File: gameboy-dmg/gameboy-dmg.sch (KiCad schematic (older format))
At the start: 32 parts, among them J1 Conn_01x02, J2 Conn_01x02, J3 Conn_01x08, J4 Conn_01x02, J5 Raspberry_Pi_2_3, J6 Conn_01x09, J8 Conn_01x02, SW1 SW_DIP_x01, U1 MCP23017_SO

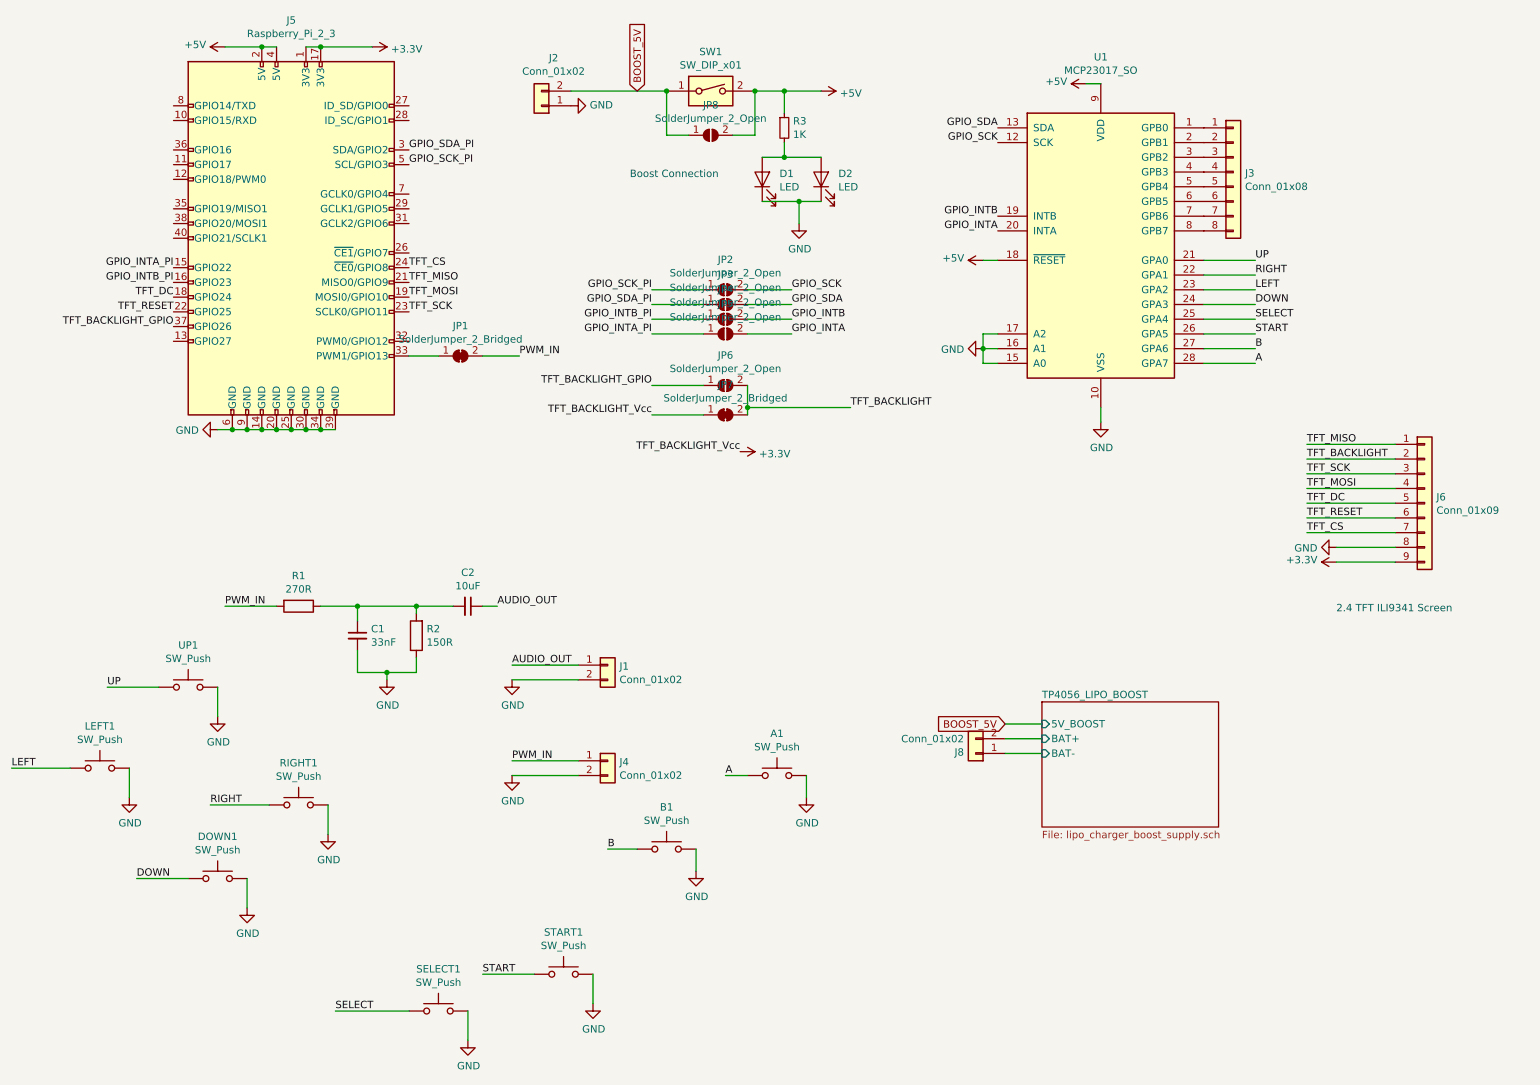
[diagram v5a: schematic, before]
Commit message: Moved buttons and audio to individual sheets and added audio amp
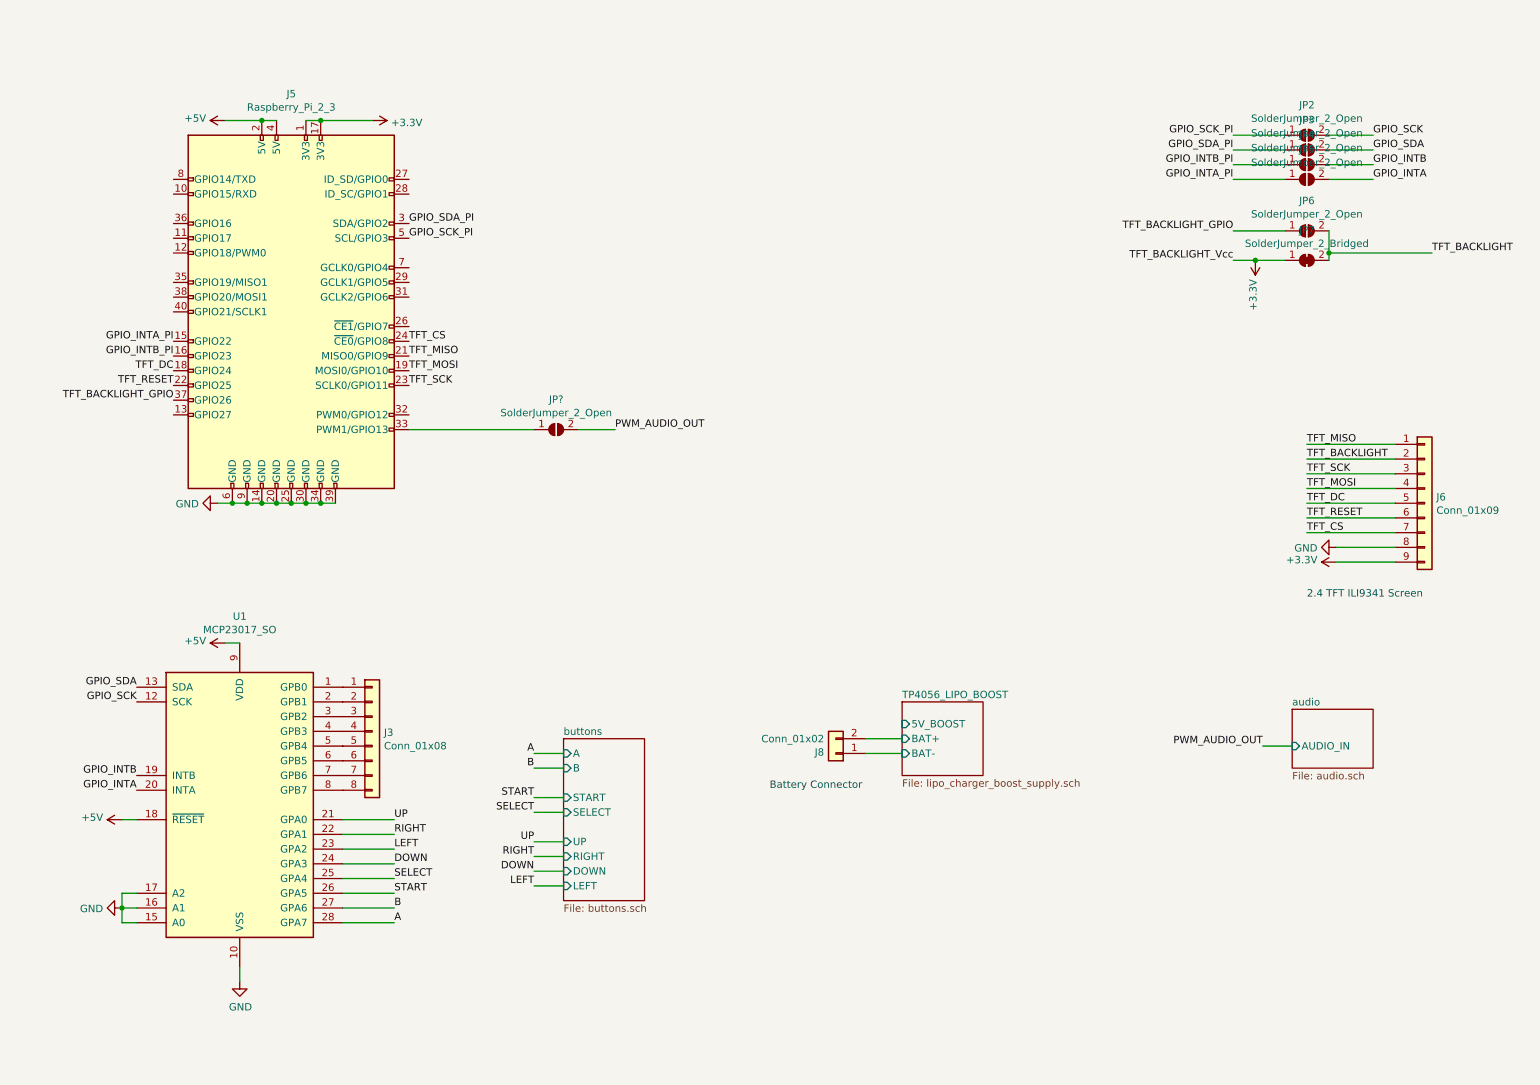
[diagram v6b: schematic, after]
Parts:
- removed A1, B1, DOWN1, LEFT1, RIGHT1, UP1: SW_Push, pad:GAMEBOY_BUTTON_PAD-D6MM, symbol Switch:SW_Push
- removed C1: 33nF, Capacitor_SMD:C_0603_1608Metric, symbol Device:C_Small
- removed C2: 10uF, Capacitor_THT:CP_Radial_D5.0mm_P2.00mm, symbol Device:C_Small
- removed D1: LED, LED_SMD:LED_0603_1608Metric, symbol Device:LED
- removed D2: LED, LED_THT:LED_D3.0mm, symbol Device:LED
- removed J1, J2, J4: Conn_01x02, Connector_PinHeader_2.54mm:PinHeader_1x02_P2.54mm_Vertical, symbol Connector_Generic:Conn_01x02
- removed JP1: SolderJumper_2_Bridged, Jumper:SolderJumper-2_P1.3mm_Bridged_RoundedPad1.0x1.5mm, symbol Jumper:SolderJumper_2_Bridged
- removed JP8: SolderJumper_2_Open, Jumper:SolderJumper-2_P1.3mm_Open_RoundedPad1.0x1.5mm, symbol Jumper:SolderJumper_2_Open
- removed R1: 270R, Resistor_SMD:R_0603_1608Metric, symbol Device:R
- removed R2: 150R, Resistor_SMD:R_0603_1608Metric, symbol Device:R
- removed R3: 1K, Resistor_SMD:R_0603_1608Metric, symbol Device:R_Small
- removed SELECT1, START1: SW_Push, pad:GAMEBOY_BUTTON_PAD-DUAL_D4MM, symbol Switch:SW_Push
- removed SW1: SW_DIP_x01, Connector_PinHeader_2.54mm:PinHeader_1x02_P2.54mm_Vertical, symbol Switch:SW_DIP_x01
- added JP?: SolderJumper_2_Open, Jumper:SolderJumper-2_P1.3mm_Open_RoundedPad1.0x1.5mm, symbol Jumper:SolderJumper_2_Open
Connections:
- net at J5.33 (PWM1/GPIO13): now also JP?.1 (A)
- new net PWM_AUDIO_OUT: JP?.2 (B)
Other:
- note added: "Battery Connector"
- note removed: "Boost Connection"
- moved on the sheet: J3, J5, J8, JP2, JP3, JP4, JP5, JP6, JP7, U1

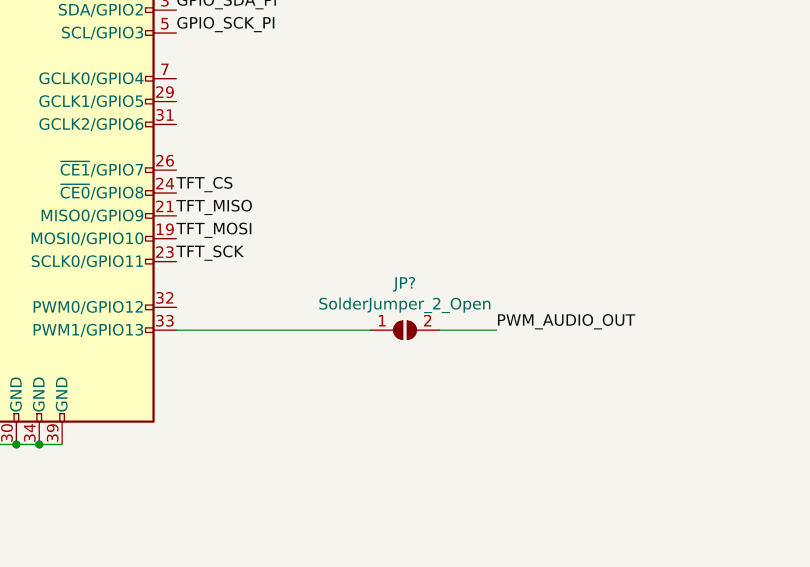
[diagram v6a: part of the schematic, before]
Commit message: Added unroputed and unchecked horizontal vol pot
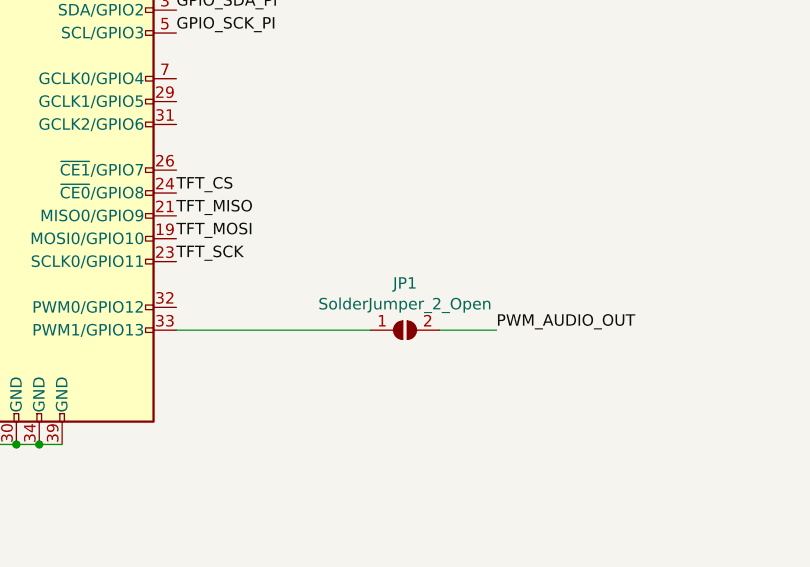
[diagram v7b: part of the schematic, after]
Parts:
- gave numbers to parts that had none: 1
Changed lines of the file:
@@
 	9050 2150 9250 2150
 $Comp
-L Jumper:SolderJumper_2_Open JP?
+L Jumper:SolderJumper_2_Open JP1
 U 1 1 5E850359
 P 4300 3300
-F 0 "JP?" H 4300 3505 50  0000 C CNN
+F 0 "JP1" H 4300 3505 50  0000 C CNN
 F 1 "SolderJumper_2_Open" H 4300 3414 50  0000 C CNN
 F 2 "Jumper:SolderJumper-2_P1.3mm_Open_RoundedPad1.0x1.5mm" H 4300 3300 50  0001 C CNN
